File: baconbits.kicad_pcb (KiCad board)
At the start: 2 copper layers, 55 x 35 mm, 64 parts, among them J1 USB_A, Q1 BC817, Q2 BC817, Q3 BC817, SW1 BTN, SW2 BTN, SW3 BTN, U1 MCP23S18-E/MJ, U2 MMA8452QR1, U3 TPD4S012DRY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

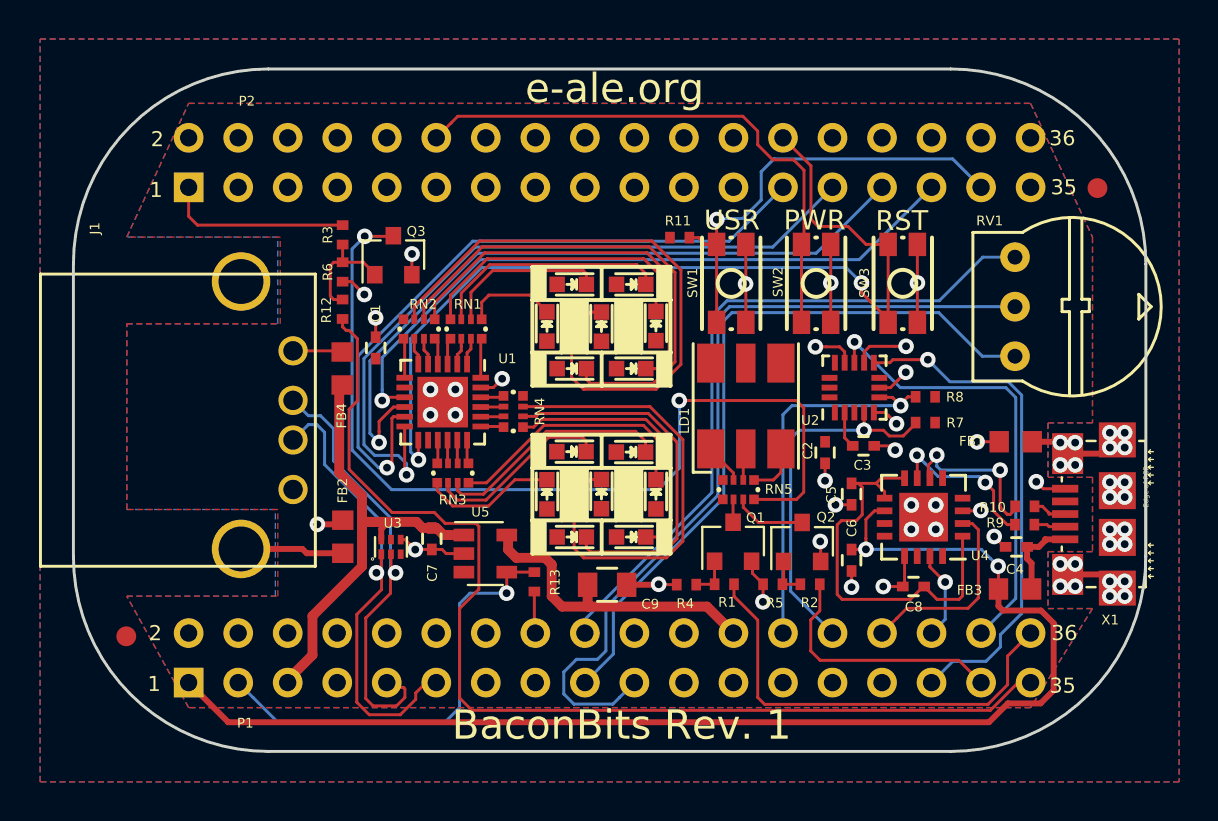
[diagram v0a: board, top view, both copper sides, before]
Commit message: R2 release for Groupgets campaign
Signed-off-by: Michael Welling <mwelling@ieee.org>
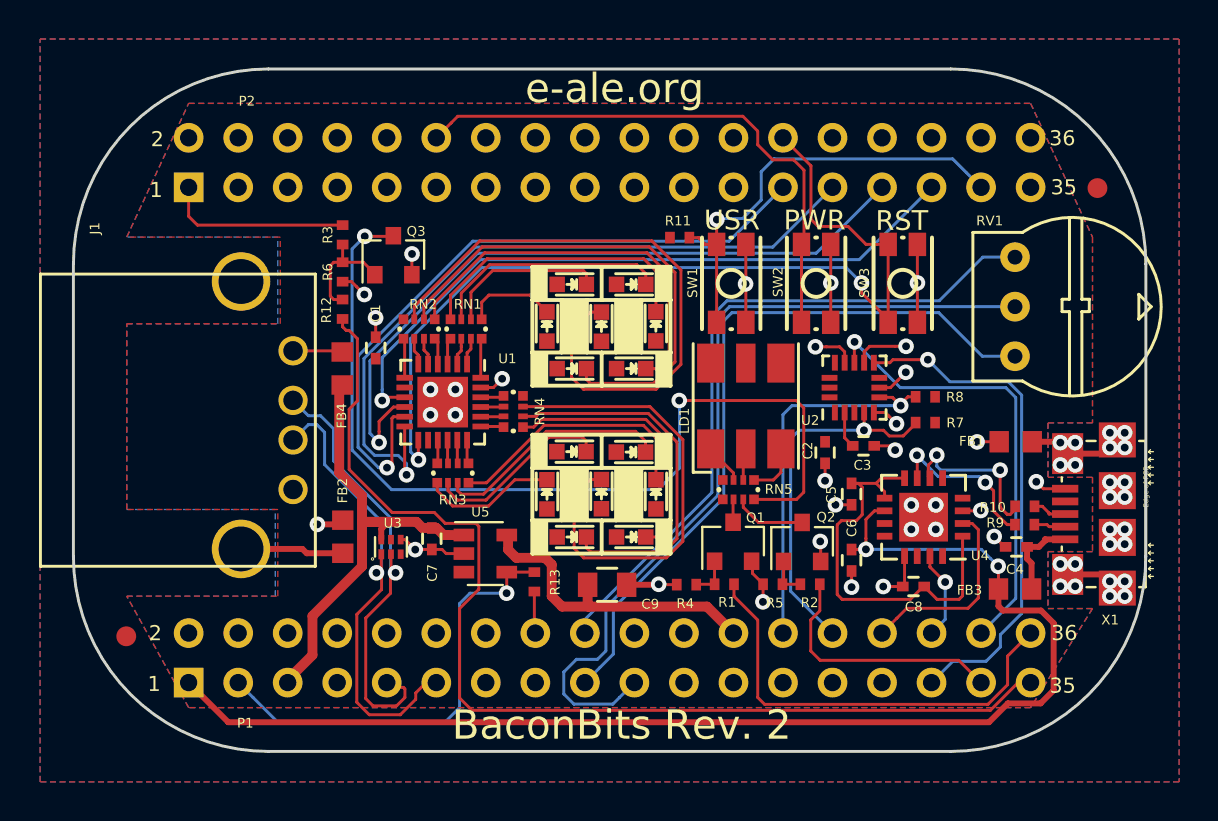
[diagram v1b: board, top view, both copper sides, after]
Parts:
- added G***: LOGO, PocketBeagle.pretty:GroupGets, B.Cu at (148.5, 100.3)
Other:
- board text added: "BaconBits Rev. 2"
- board text added: "BaconBits Rev. 2 04-20-2019"
- board text removed: "BaconBits Rev. 1"
- board text removed: "BaconBits Rev. 1 02-14-2018"
